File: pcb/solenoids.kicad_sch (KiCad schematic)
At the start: 3 parts

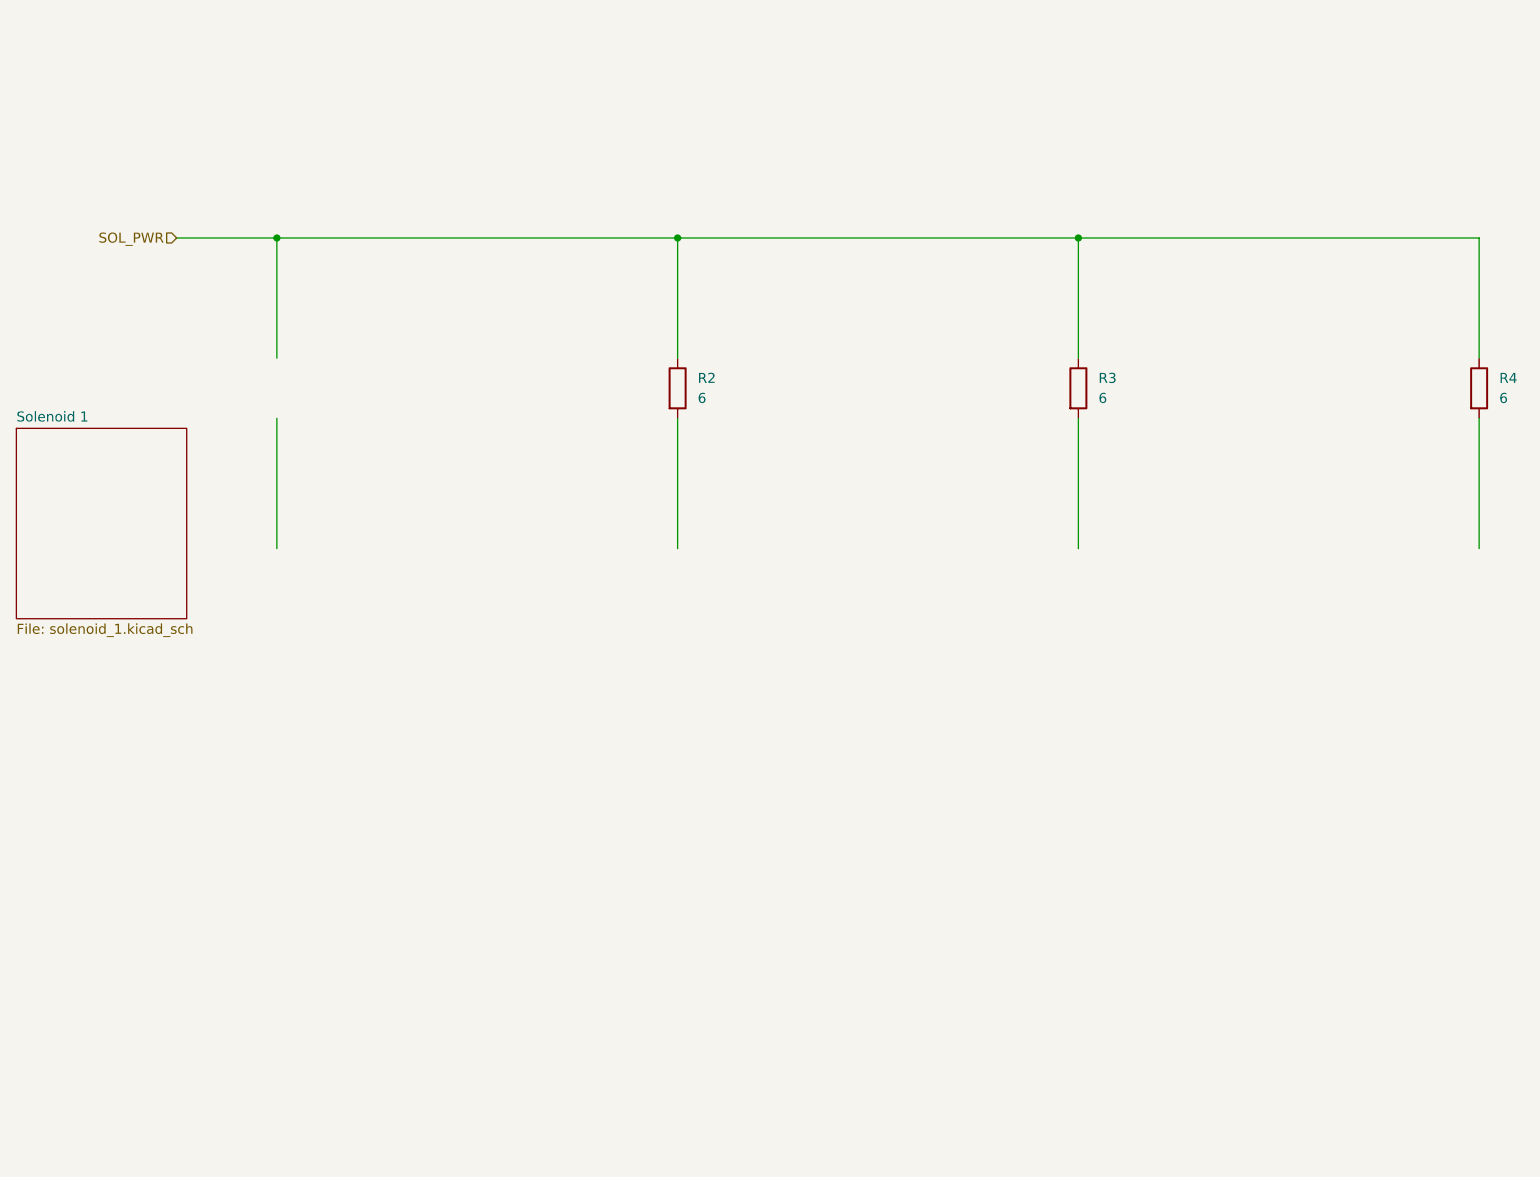
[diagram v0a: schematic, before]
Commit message: Create STM32 project, expand ADC and GPIO schematic
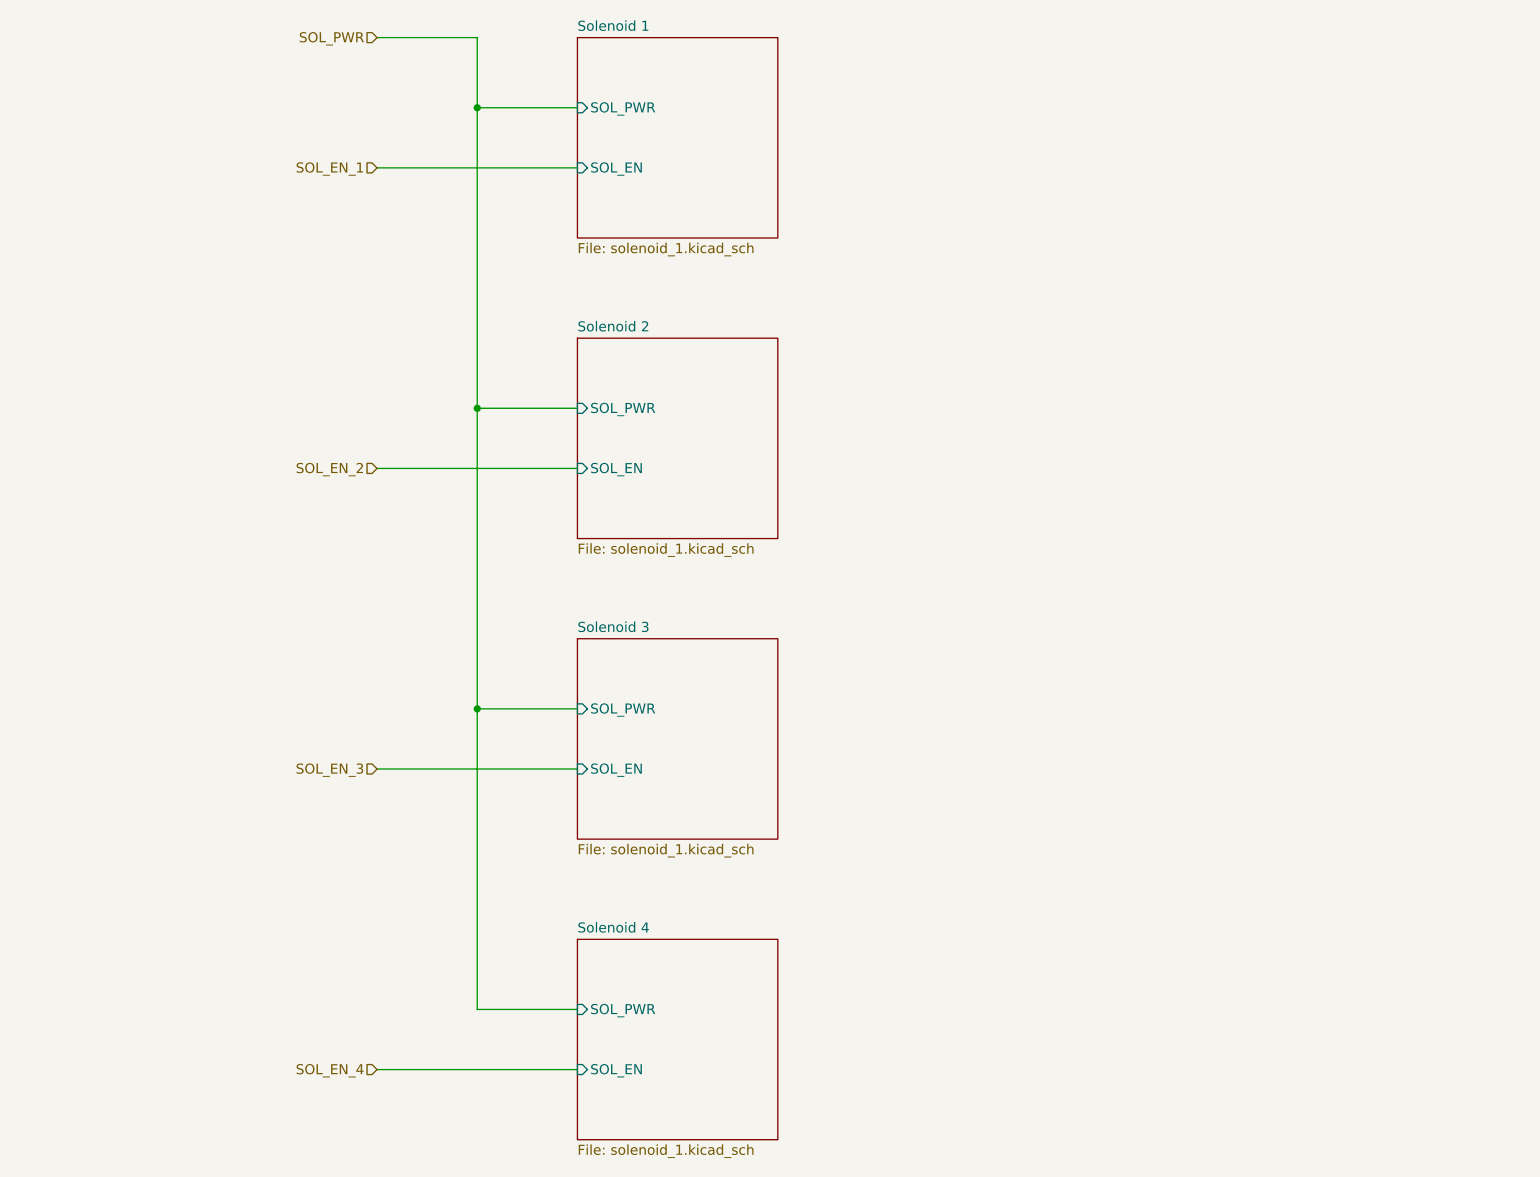
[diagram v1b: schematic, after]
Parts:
- removed R2, R3, R4: 6, symbol Device:R
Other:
- added sheet Solenoid 2 (solenoid_1.kicad_sch)
- added sheet Solenoid 3 (solenoid_1.kicad_sch)
- added sheet Solenoid 4 (solenoid_1.kicad_sch)
- sheet Solenoid 1 ports: added SOL_EN, SOL_PWR; removed none
